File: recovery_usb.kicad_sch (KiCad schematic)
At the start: 51 parts, among them J3 USB-C_Kycon_KUSBX-SL2-CS1N24-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, Q15 DMG1012T-7, Q19 DMG1012T-7, U23 AP22615A_TSOT26, U26 TPD4E05U06QDQARQ1, U56 HD3SS3220IRNHR, U57 TPD4E05U06QDQARQ1, U58 TPD4E05U06QDQARQ1

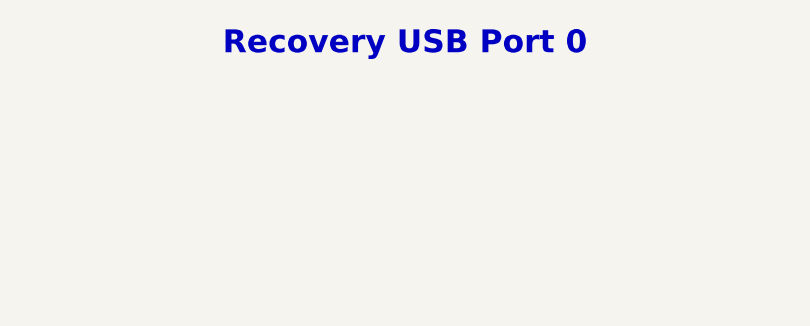
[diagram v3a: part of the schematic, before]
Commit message: [#85326] Update USB naming convention
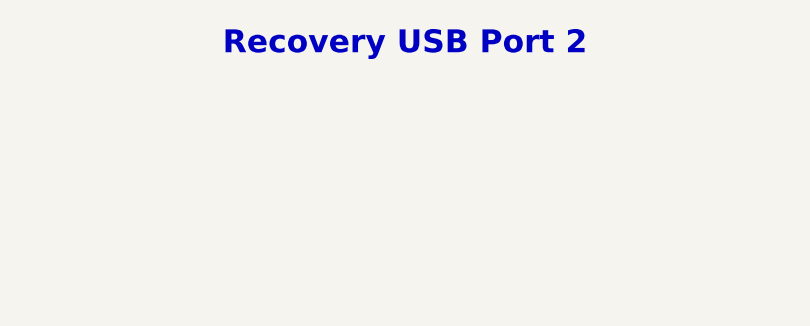
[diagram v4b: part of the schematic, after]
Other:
- note added: "Recovery USB Port 2"
- note removed: "Recovery USB Port 0"
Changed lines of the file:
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@@
 		)
 	)
-	(text "Recovery USB Port 0\n"
+	(text "Recovery USB Port 2\n"
 		(exclude_from_sim no)
 		(at 185.674 24.384 0)
@@
 		(polyline
 			(pts
-				(xy 281.305 147.955) (xy 269.24 147.955) (xy 269.24 142.24) (xy 281.305 142.24)
+				(xy 248.92 180.975) (xy 189.3887 180.975) (xy 189.23 149.86) (xy 248.92 149.86)
 			)
 			(stroke
@@
 		(polyline
 			(pts
-				(xy 248.92 180.975) (xy 189.3887 180.975) (xy 189.23 149.86) (xy 248.92 149.86)
+				(xy 281.305 147.955) (xy 269.24 147.955) (xy 269.24 142.24) (xy 281.305 142.24)
 			)
 			(stroke

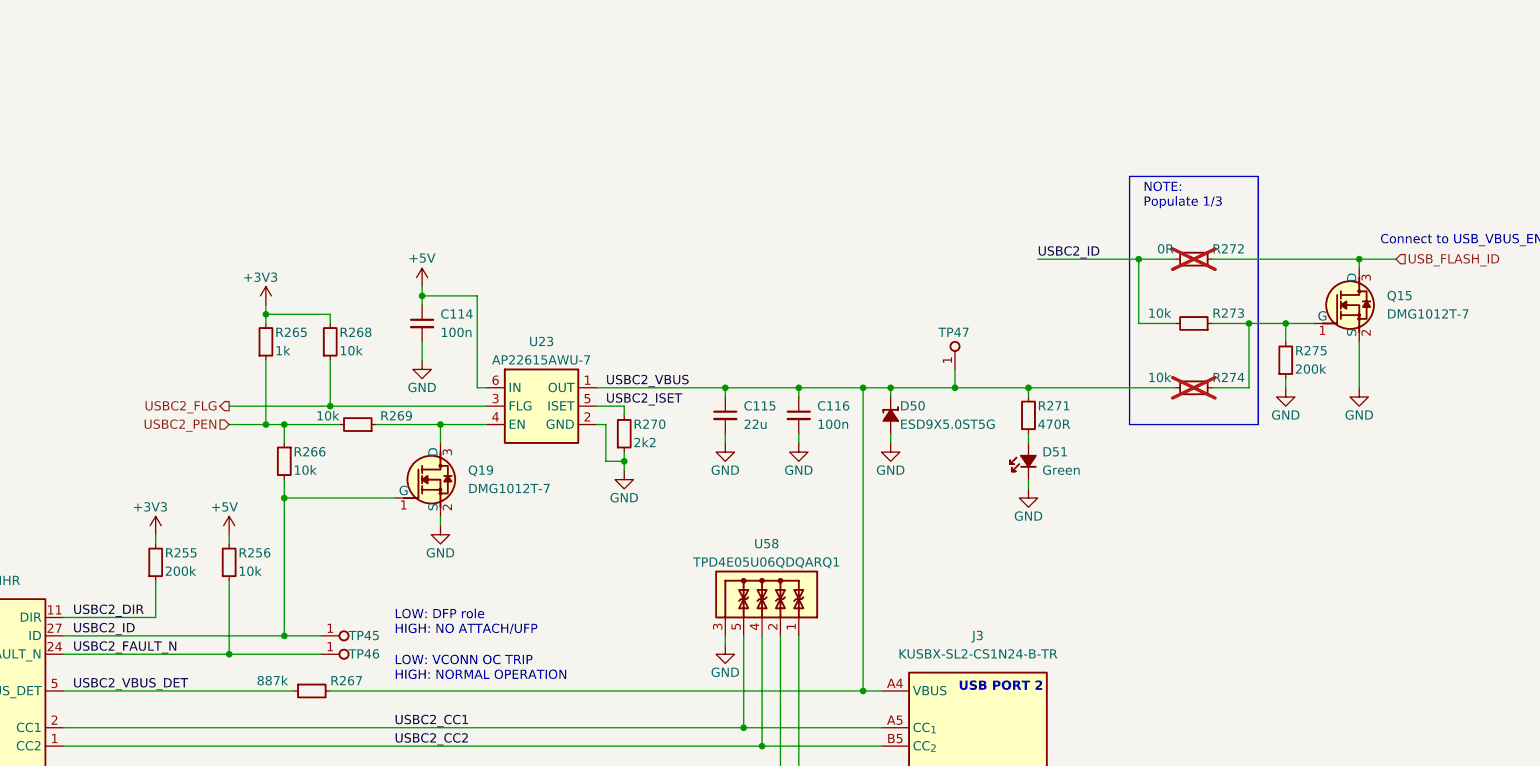
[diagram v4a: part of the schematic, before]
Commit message: [#85326] Fix USB-C 2 ID and enable handling
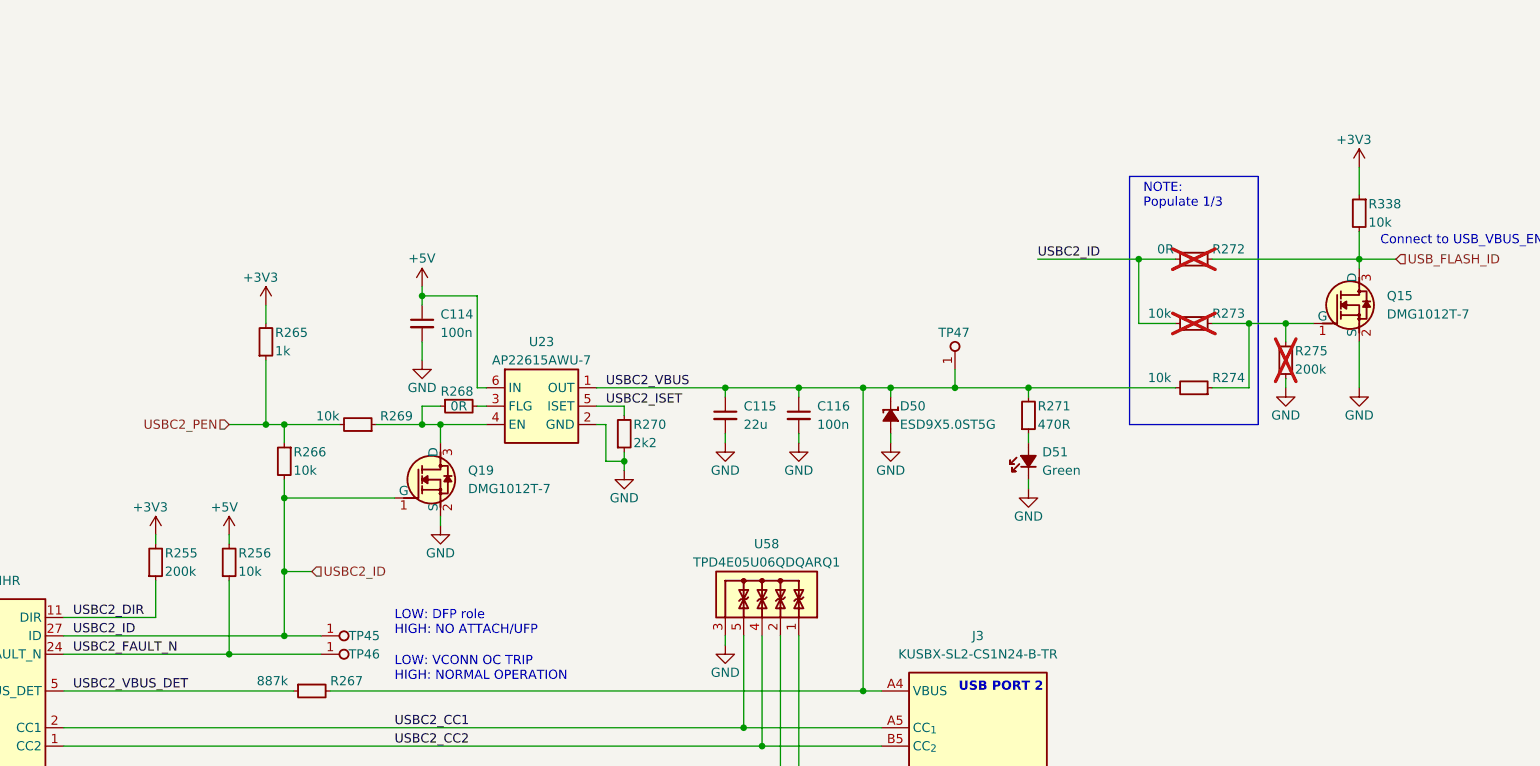
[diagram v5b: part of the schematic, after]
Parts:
- removed R268: R_10k_0402, antmicro-footprints:R_0402_1005Metric, symbol antmicroResistors0402:R_10k_0402
- added R268: R_0R_0402, antmicro-footprints:R_0402_1005Metric, symbol antmicroResistors0402:R_0R_0402
- added R338: R_10k_0402, antmicro-footprints:R_0402_1005Metric, symbol antmicroResistors0402:R_10k_0402
- R273, R275: now not fitted; now left out of the parts list
- R274: now fitted; now in the parts list
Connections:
- net +3V3: now also R338.1
- net USB_FLASH_ID: now also R338.2
- net at Q19.3 (D), R269.1, U23.4 (EN): now also R268.1
- net USBC2_FLG: no longer names the net of U23.3 (FLG)
- net USBC2_FLG: now also R268.2

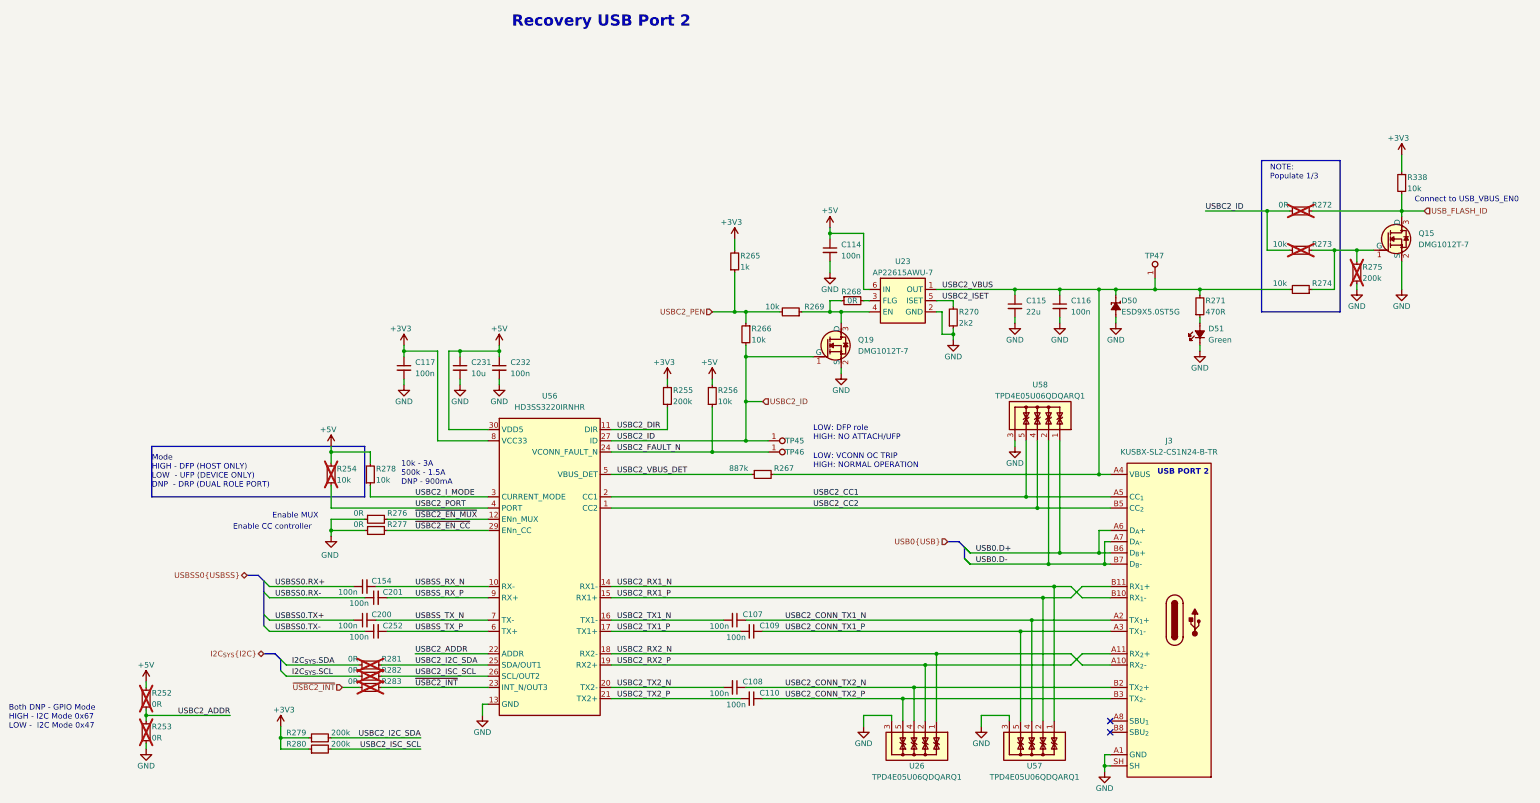
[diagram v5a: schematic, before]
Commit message: [#85326] Improved USB-C 2 control signal connections
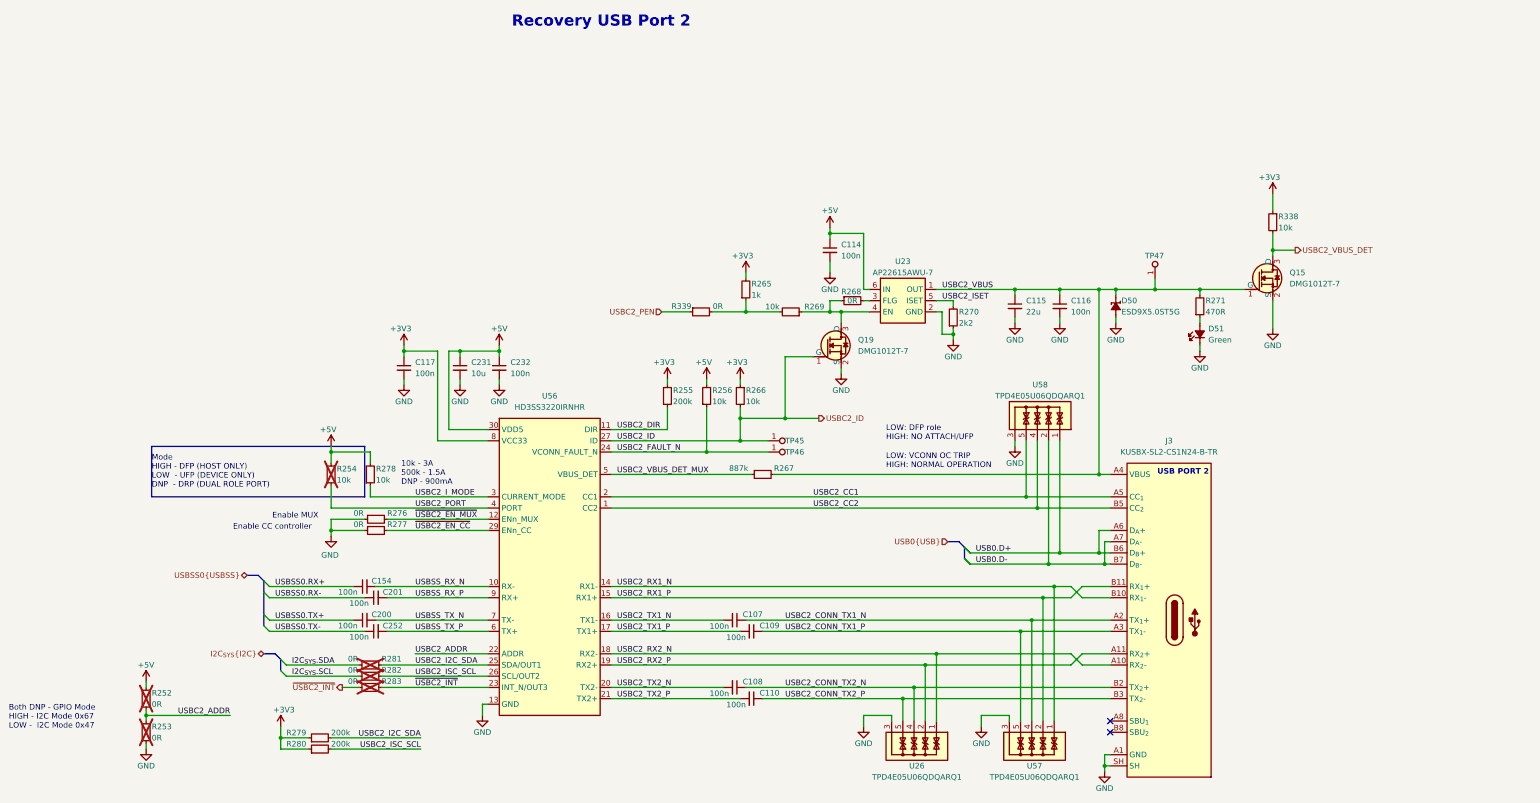
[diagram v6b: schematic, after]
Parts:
- removed R272: R_0R_0402, antmicro-footprints:R_0402_1005Metric, symbol antmicroResistors0402:R_0R_0402
- removed R273, R274: R_10k_0402, antmicro-footprints:R_0402_1005Metric, symbol antmicroResistors0402:R_10k_0402
- removed R275: R_200k_0402, antmicro-footprints:R_0402_1005Metric, symbol antmicroResistors0402:R_200k_0402
- added R339: R_0R_0402, antmicro-footprints:R_0402_1005Metric, symbol antmicroResistors0402:R_0R_0402
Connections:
- net USB_FLASH_ID is gone; now on net USBC2_VBUS_DET: Q15.3 (D), R338.2
- net +3V3: now also R266.1
- net USBC2_PEN: now also R339.1; no longer R265.1, R266.1, R269.2
- net USBC2_VBUS: now also Q15.1 (G)
- net USBC2_VBUS_DET: no longer R267.1, U56.5 (VBUS_DET)
- new net: R265.1, R269.2, R339.2
- new net USBC2_VBUS_DET_MUX: R267.1, U56.5 (VBUS_DET)
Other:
- note removed: "Connect to USB_VBUS_EN0"
- note removed: "NOTE: Populate 1/3"
- moved on the sheet: Q15, R256, R265, R266, R338

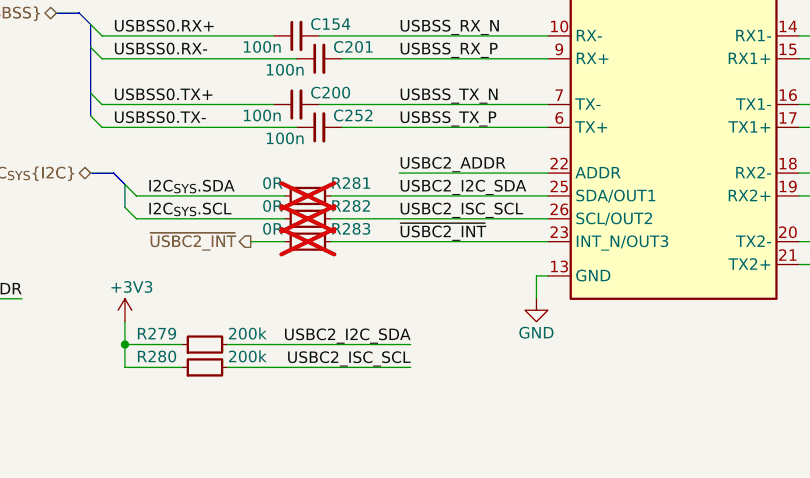
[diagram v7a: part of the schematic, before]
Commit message: [#85326] Change SFP+ to SFP28; minor corrections to sch
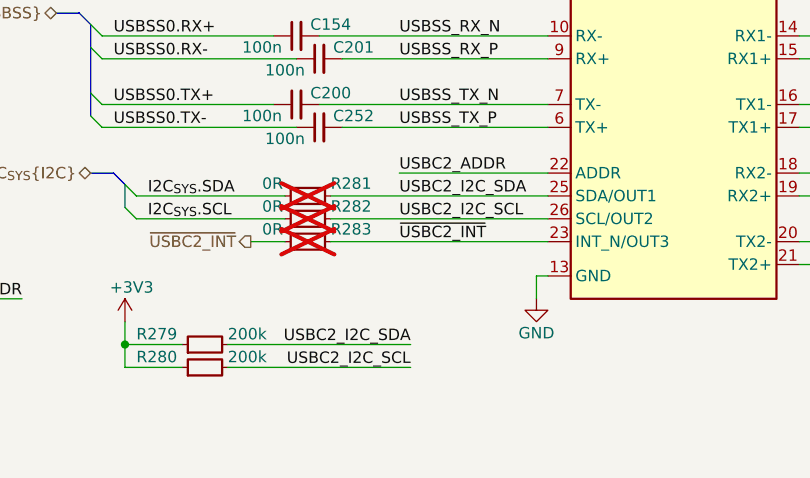
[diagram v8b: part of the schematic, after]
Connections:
- net USBC2_ISC_SCL renamed USBC2_I2C_SCL
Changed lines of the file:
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@@
 	(title_block
 		(title "Jetson AGX Thor Baseboard")
-		(date "2025-10-21")
+		(date "2025-10-22")
 		(rev "1.0.0")
 		(company "Antmicro Ltd")
@@
 		)
 	)
-	(label "USBC2_ISC_SCL"
+	(label "USBC2_I2C_SCL"
 		(at 144.78 189.23 180)
 		(effects
@@
 		)
 	)
-	(label "USBC2_ISC_SCL"
+	(label "USBC2_I2C_SCL"
 		(at 143.51 172.72 0)
 		(effects
